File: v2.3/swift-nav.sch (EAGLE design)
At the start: 171 parts, among them J1 SMA_EDGE, J6 ZX62-B-5PA, Q1 IRLML6401, U1 6SLX9FTG256, U10 MAX2769, U12 PT7M8206B33TA5EX, U13 M25PX80, U2 LTC3407A_DFN, U3 STM32-M-64-LQFP, U4 7Q-16.368MBG-T, U5 SMA_PATCH, U6 93LC56BT-I/OT, U7 FT232HQ, U8 B4050, X4 NX5032GA-12M, X5 CONN_5-2

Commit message: Added extra pages and partitioned design amongst pages to make it more neat. Snapped components and connections to grid where they weren't 100 mil snapped.
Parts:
- removed U$1: LOGOINITIALS, swift-nav:LOGOINITIALS
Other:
- note added: "2.3"
- note added: "Connectors / Misc"
- note added: "Digital Power"
- note added: "FPGA IO / JTAG / FLASH"
- note added: "FPGA Power Pins / Bypassing"
- note added: "FTDI UART/FIFO to USB"
- note added: "Fiducials"
- note added: "Microcontroller"
- note added: "Mounting Holes"
- note added: "RF Frontend / RF Power"
- note added: "RF shield"
- note added: "Spartan Configuration Flash"
- note added: "Spartan JTAG"
- note removed: "2.2"
- note removed: "FPGA / POWER / RF"
- note removed: "FPGA_DEBUG_HDR"
- note removed: "Inner RF Shield"
- note removed: "Outer RF shield"
- note removed: "STM32 / CONNECTORS"
- note removed: "Spartan Configuration"

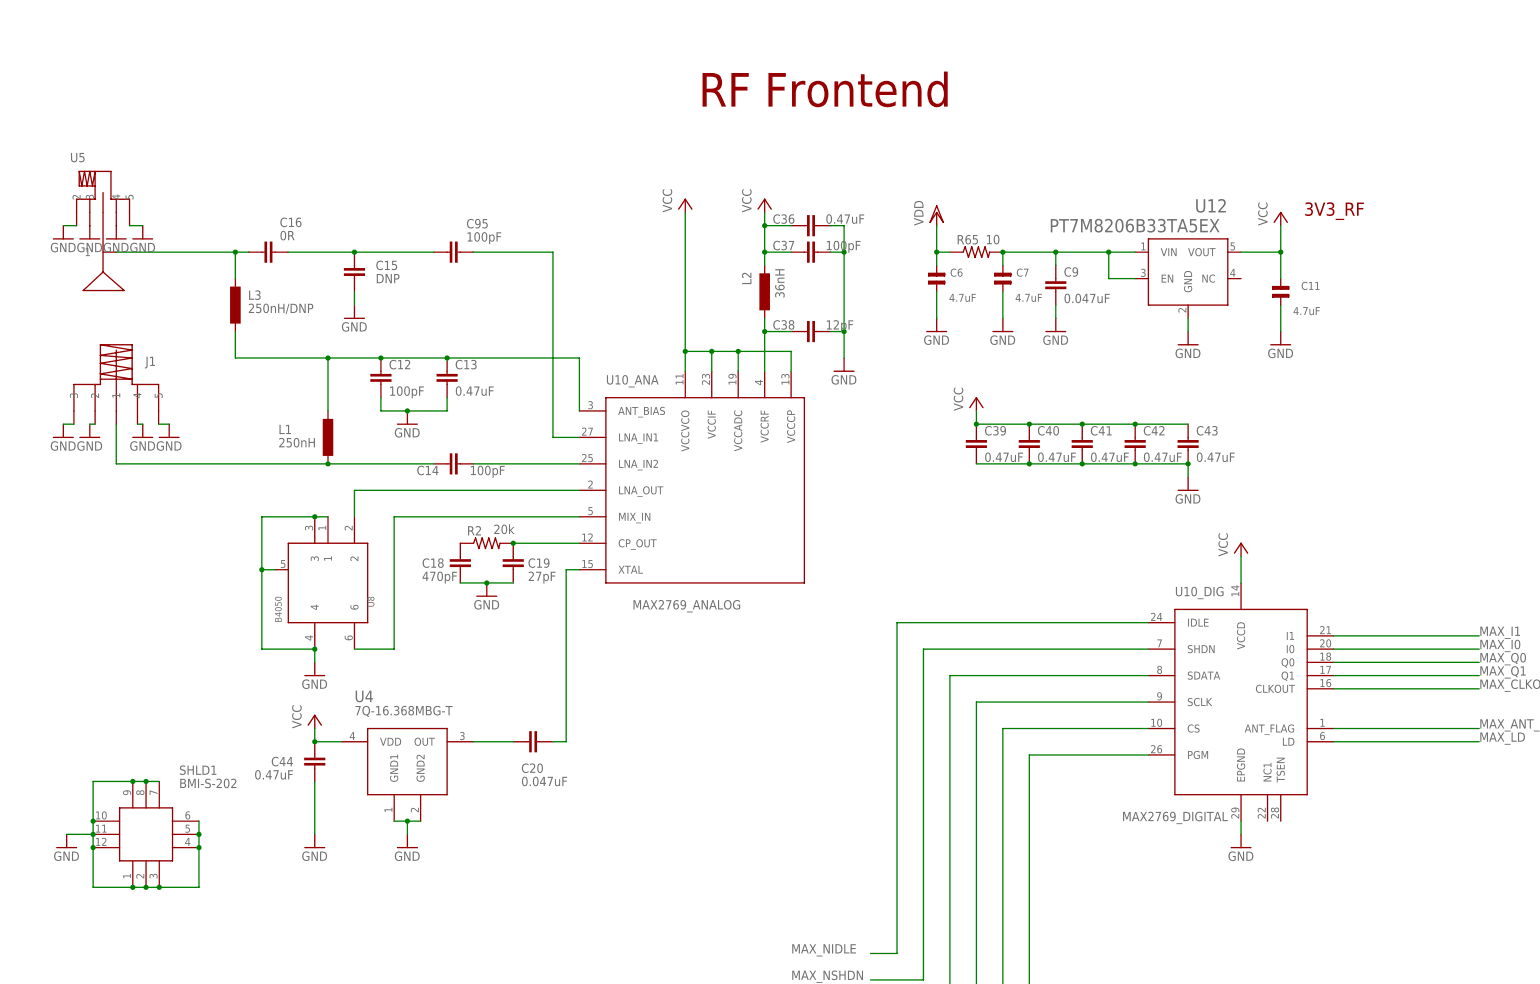
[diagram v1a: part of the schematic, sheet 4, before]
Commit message: In schematic: -Resistor between V_USB and STM USB detect pin -Add more FIFO lines from FPGA -Removed internal shield -Added LNA and associated components to LNA1 line -Changed LNA1 SMA to 1 thru hole signal 4 SMD GND pads -Changed digital supplies on MAX (TCXO, ADC, VDD_D) to digital 3V3 In board: -Changed patch position to center of board
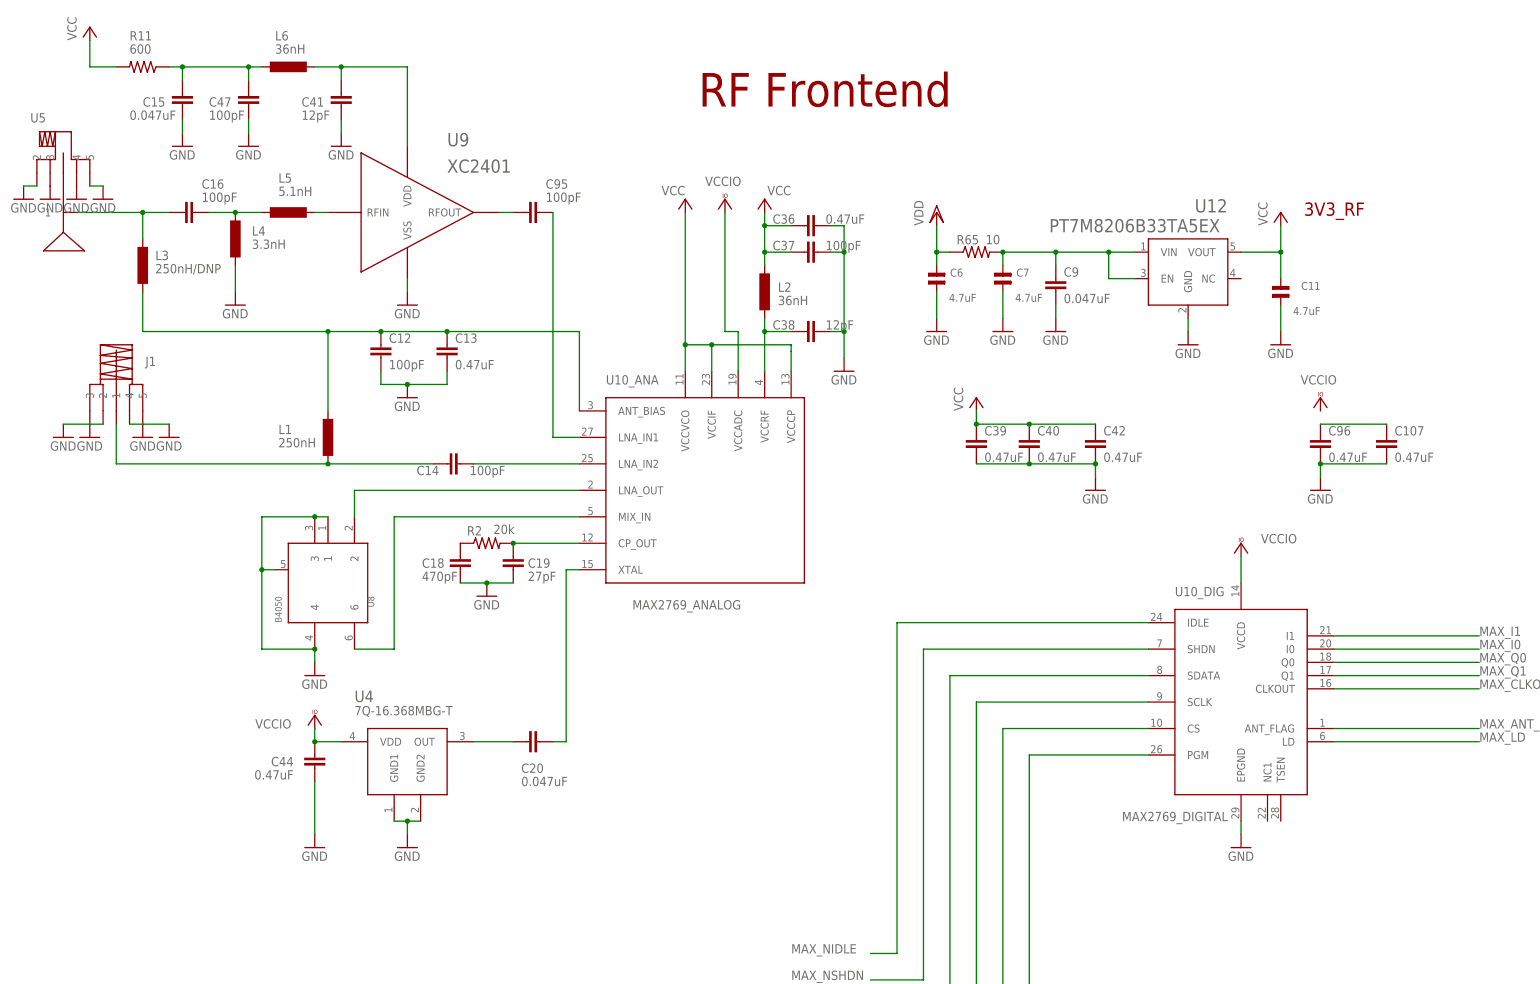
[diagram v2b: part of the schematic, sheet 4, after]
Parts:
- removed C43: 0.47uF, rcl:C-EUC0402
- removed SHLD1: BMI-S-202, jobygnss:BMI-S-202
- removed SJ1: SOLDERJUMPERTRACE, SparkFun-Passives:SOLDERJUMPERTRACE
- added C107, C96: 0.47uF, rcl:C-EUC0402
- added C47: 100pF, rcl:C-EUC0402
- added L4: 3.3nH, pel_dipol_comp:INDUCTOR-0402
- added L5: 5.1nH, pel_dipol_comp:INDUCTOR-0402
- added L6: 36nH, pel_dipol_comp:INDUCTOR-0402
- added R10: 10K, pel_dipol_comp:RESISTOR-0402
- added R11: 600, rcl:R-US_R0402
- added U9: XC2401, swift-nav:XC2401
- C15: value DNP -> 0.047uF
- C16: value 0R -> 100pF
- C41: value 0.47uF -> 12pF
- U5: value SMA_PATCH -> SMA_PATCH_SMDGND; device joby_robotics:SMA_PATCH -> joby_robotics:SMA_PATCH_SMDGND
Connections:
- removed net UART6_RX: U3.PC7-TIM3CH2, U7.AD0
- removed net UART6_TX: SJ1.2, U3.PC6-TIM3CH1
- new net FTDI_ADBUS2: U1B1.IO_L50N_M1UDQSN_1, U7.AD2
- new net FTDI_ADBUS3: U1B1.IO_L49P_M1DQ10_1, U7.AD3
- new net FTDI_ADBUS4: U1B1.IO_L48N_M1DQ9_1, U7.AD4
- new net N$18: R10.1, U3.PB0-ADC8/TIM3CH3-TIM1CH2N
- new net N$36: C95.1, U9.RFOUT
- new net N$37: C15.2, C47.2, L6.2, R11.1
- new net N$38: U10_ANA.VCCCP
- new net N$41: C41.2, L6.1, U9.VDD
- new net N$42: C107.1, C96.1
- new net UART6_RX/FTDI_ADBUS0: U1B1.IO_L37P_A7_M1A0_1, U3.PC7-TIM3CH2, U7.AD0
- new net UART6_TX/FTDI_ADBUS1: U1B1.IO_L36N_A8_M1BA1_1, U3.PC6-TIM3CH1, U7.AD1
- net GND: now also C107.2, C41.1, C47.1, C96.2, L4.1, U9.VSS; no longer C41.2, C43.2, SHLD1.P$1, SHLD1.P$10, SHLD1.P$11, SHLD1.P$12, SHLD1.P$2, SHLD1.P$3, SHLD1.P$4, SHLD1.P$5, SHLD1.P$6, SHLD1.P$7, SHLD1.P$8, SHLD1.P$9
- net N$14: now also C16.1; no longer C16.2
- net N$2: now also L5.1, U9.RFIN; no longer SJ1.1, U7.AD1
- net N$35: now also C16.2, L4.2, L5.2; no longer C15.2, C16.1, C95.1
- net VCC: now also R11.2; no longer C41.1, C43.1, C44.1, U10_ANA.VCCADC, U10_ANA.VCCCP, U10_DIG.VCCD, U4.VDD
- net VCCIO: now also C44.1, U10_ANA.VCCADC, U10_DIG.VCCD, U4.VDD
- net V_USB: now also R10.2; no longer U3.PB0-ADC8/TIM3CH3-TIM1CH2N
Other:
- moved on the sheet: C12, C13, C15, C16, C41, C42, C95, L3, U5

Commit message: Cleaned up RF section a little bit. Going to split MAX2769 symbol up a little bit more to clean it up further.
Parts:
- removed L6: 36nH, pel_dipol_comp:INDUCTOR-0402
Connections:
- removed net N$37: C15.2, C47.2, L6.2, R11.1
- removed net N$42: C107.1, C96.1
- net N$41: now also C15.2, C47.2, R11.1; no longer L6.1
- net VCCIO: now also C107.1, C96.1
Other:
- note added: "Bypassing"
- note added: "RF Frontend - Analog Section"
- note added: "RF Frontend - Digital Section"
- note added: "RF LDO Regulator"
- note removed: "RF Frontend"
- moved on the sheet: C107, C11, C15, C39, C40, C42, C47, C6, C7, C9, C96, J1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

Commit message: Cleaned up RF section a bit more - separated max2769 into 3 symbols
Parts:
- L1: value 250nH -> 29nH
- L2: value 36nH -> 29nH
- L3: value 250nH/DNP -> 29nH
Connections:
- removed net N$10: C12.1, C13.1, L1.2, L3.1, U10_ANA.ANT_BIAS
- removed net N$38: U10_ANA.VCCCP
- new net N$37: C12.2, C13.2, L1.1, L3.2, U10_ANA.ANT_BIAS
- net GND: now also C12.1, C13.1, U10_PWR.EPGND; no longer C12.2, C13.2, U10_DIG.EPGND
- net MAX_CLKOUT: now also U10_DIG.CLK_OUT; no longer U10_DIG.CLKOUT
- net MAX_NIDLE: now also U10_DIG.!IDLE; no longer U10_DIG.IDLE
- net MAX_NSHDN: now also U10_DIG.!SHDN; no longer U10_DIG.SHDN
- net N$14: now also L1.2; no longer L3.2
- net N$22: now also U10_PWR.VCCRF; no longer U10_ANA.VCCRF
- net N$8: now also L3.1; no longer L1.1
- net SPI2NSS_MAX: now also U10_DIG.!CS; no longer U10_DIG.CS
- net VCC: now also U10_PWR.VCCCP, U10_PWR.VCCIF, U10_PWR.VCCVCO; no longer U10_ANA.VCCIF, U10_ANA.VCCVCO
- net VCCIO: now also U10_PWR.VCCADC, U10_PWR.VCCD; no longer U10_ANA.VCCADC, U10_DIG.VCCD
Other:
- note added: "RF Frontend - Power"
- note added: "RF Frontend Power Bypassing"
- note removed: "Bypassing"
- moved on the sheet: C107, C11, C12, C13, C14, C15, C16, C18, C19, C20, C36, C37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

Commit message: Added pull up resistors to NIDLE and NSHDN and pull down to PGM
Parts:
- removed C41: 12pF, rcl:C-EUC0402
- added R12, R19, R20: 10k, rcl:R-US_R0402
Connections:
- net GND: now also R20.1; no longer C41.1
- net MAX_NIDLE: now also R12.1
- net MAX_NSHDN: now also R19.1
- net MAX_PGM: now also R20.2
- net N$41: no longer C41.2
- net VCCIO: now also R12.2, R19.2
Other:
- moved on the sheet: C107, C15, C39, C40, C42, C47, C51, C52, C53, C54, C55, C96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

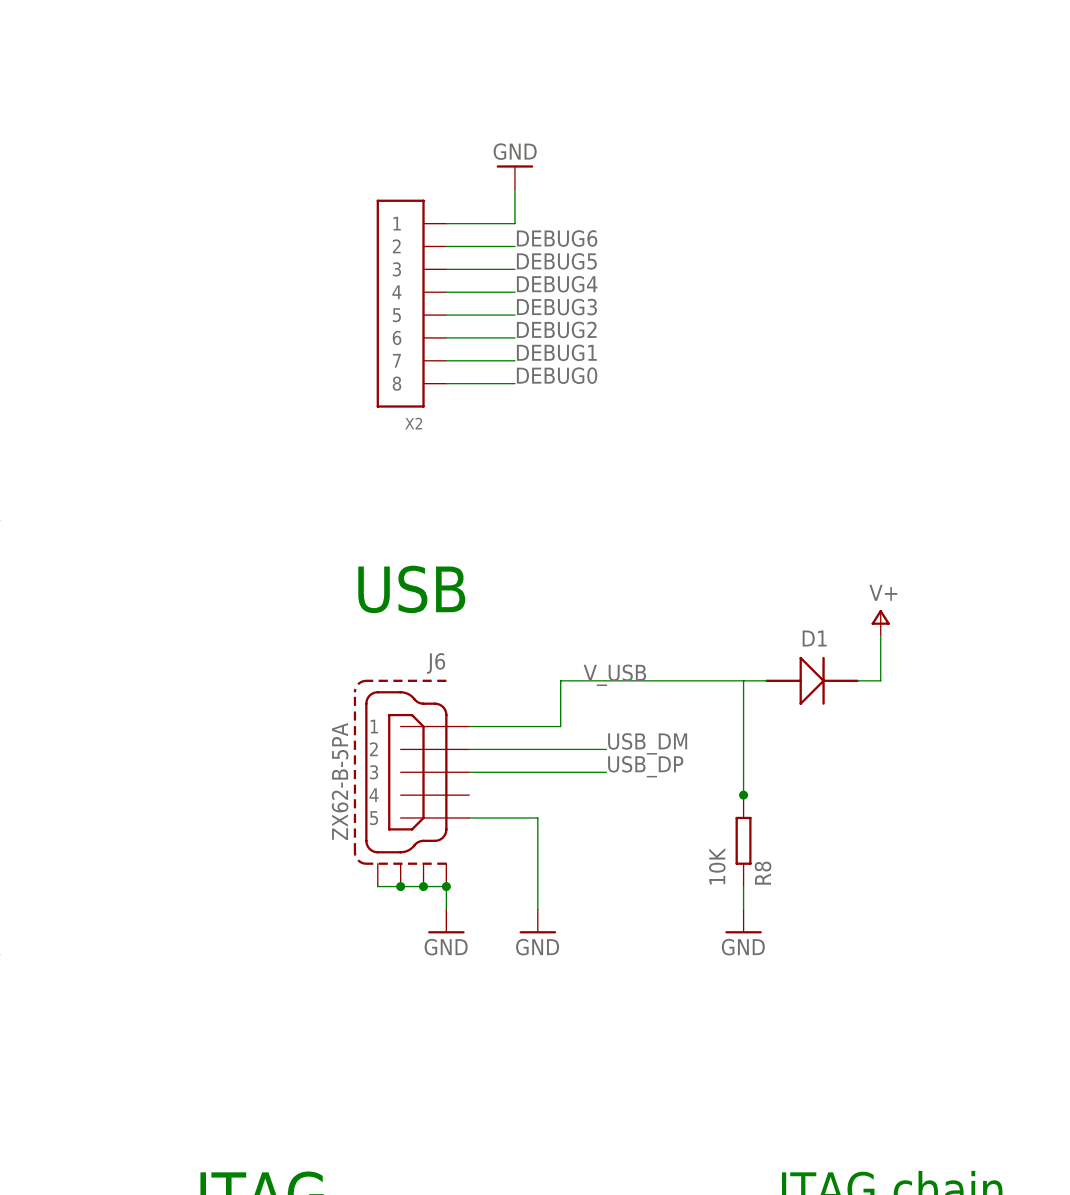
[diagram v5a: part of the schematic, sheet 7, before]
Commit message: Changed debug header to 12 pin with 1 gnd 1 VDD and 10 signal connections
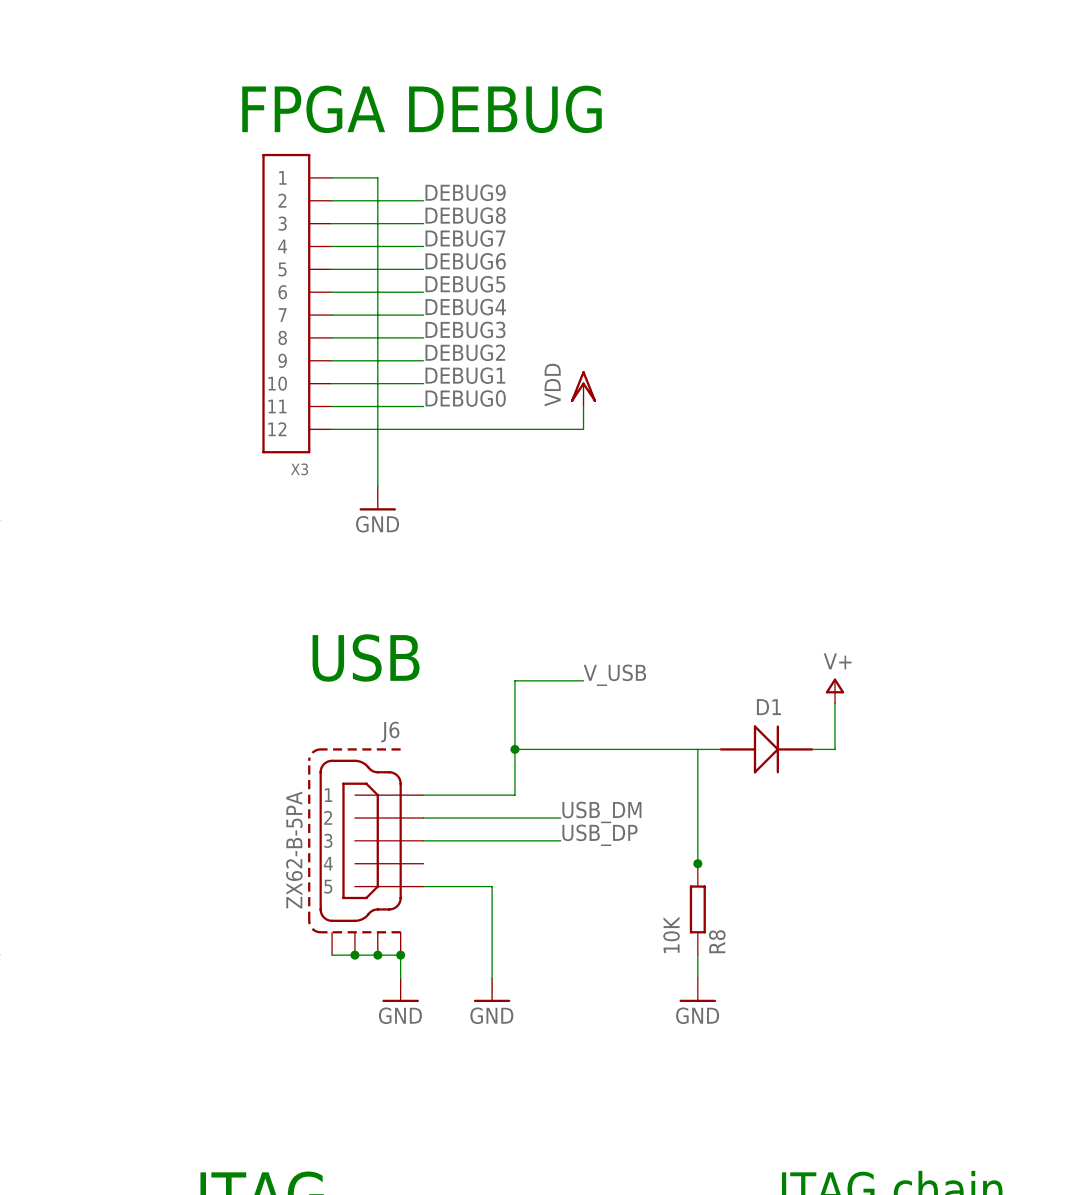
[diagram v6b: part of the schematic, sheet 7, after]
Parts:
- removed X2: (no value), pel_molex:CONN_8-1-53261
- added X3: FPGA DEBUG, pel_molex:CONN_12-1-53261
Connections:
- new net DEBUG7: X3.4
- new net DEBUG8: X3.3
- new net DEBUG9: X3.2
- net DEBUG0: now also X3.11; no longer X2.8
- net DEBUG1: now also X3.10; no longer X2.7
- net DEBUG2: now also X3.9; no longer X2.6
- net DEBUG3: now also X3.8; no longer X2.5
- net DEBUG4: now also X3.7; no longer X2.4
- net DEBUG5: now also X3.6; no longer X2.3
- net DEBUG6: now also X3.5; no longer X2.2
- net GND: now also X3.1; no longer X2.1
- net VDD: now also X3.12
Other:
- moved on the sheet: D1, J6, R8
